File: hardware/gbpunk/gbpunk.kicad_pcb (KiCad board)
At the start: 2 copper layers, 57.5 x 82 mm, 61 parts, among them J1 CART, J2 SWD_CONNECTOR, J4 SWD_CONNECTOR, P1 USB_C_CONNECTOR, SW7 RESET, SW9 USB_BOOT, U1 RP2040, U2 SN74LVC4245A, U3 W25Q128JVS, U4 NCP1117-3.3_SOT223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

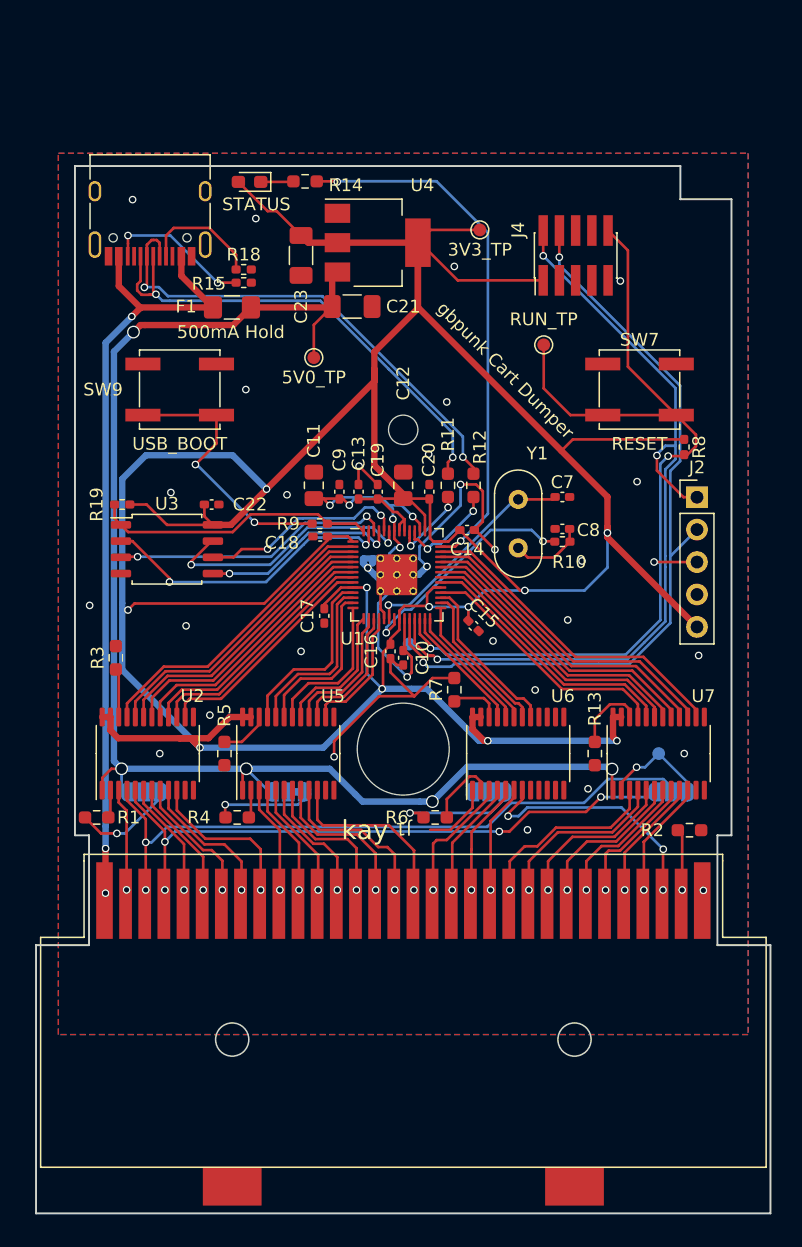
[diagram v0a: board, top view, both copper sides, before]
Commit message: big PCB reroute so the connector is not upside down
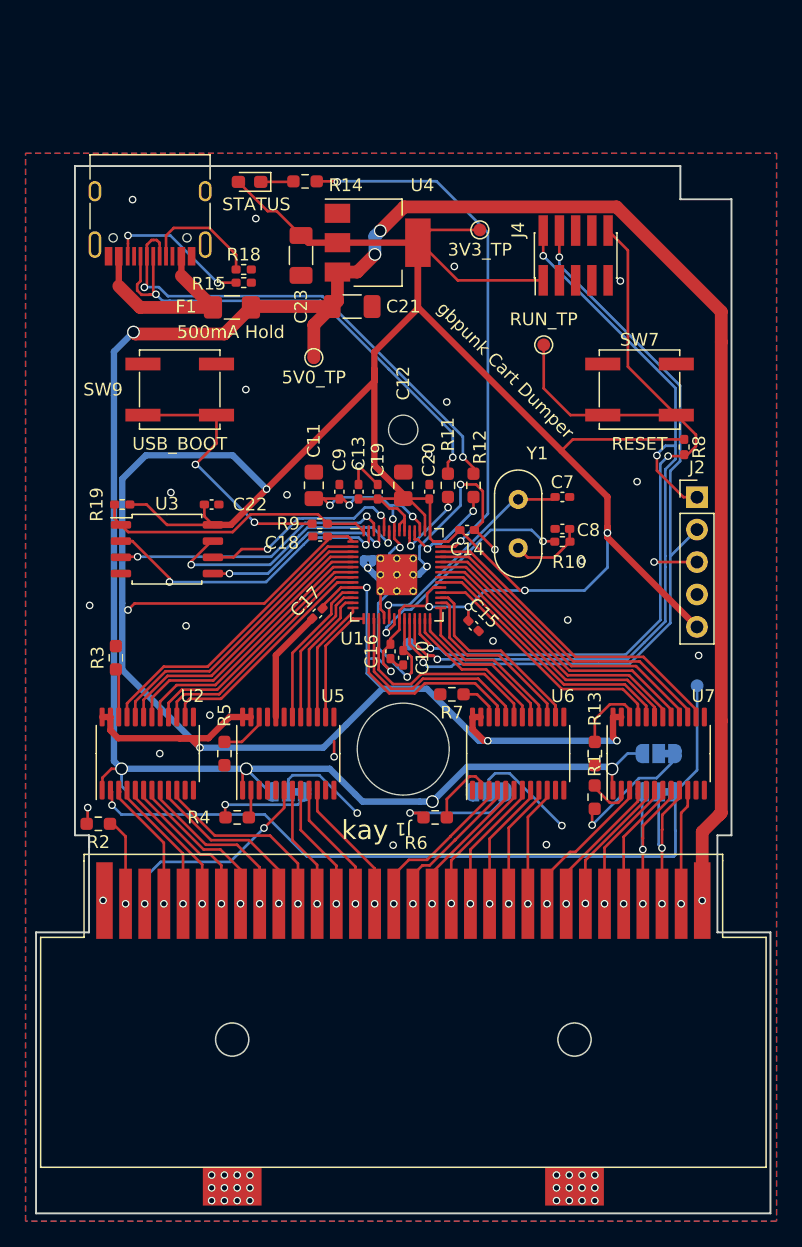
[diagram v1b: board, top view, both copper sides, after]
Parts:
- moved R2 46.3 mm to (76.1, 90.5)
- moved JP2 40.4 mm to (120.0, 85.0)
- moved R1 39.0 mm to (115.0, 88.4), turned to -90 degrees
- moved TP4 6.10 mm to (123.0, 79.7)
- moved JP1 1.00 mm to (120.0, 88.0)
- moved C17 0.57 mm to (93.3, 74.0), turned to -135 degrees
- moved R7 0.41 mm to (103.8, 80.4), turned to 180 degrees
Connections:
- J1 pad 1: VBUS -> +5V
- R2 pad 1: GND -> Net-(J1-Pad31)
- R2 pad 2: Net-(J1-Pad31) -> GND
- U1 pad 11: /A4_L -> /RST_L
- U1 pad 12: /A5_L -> /A15_L
- U1 pad 13: /A6_L -> /A14_L
- U1 pad 14: /A7_L -> /A13_L
- U1 pad 15: /A8_L -> /A12_L
- U1 pad 16: /A9_L -> /A11_L
- U1 pad 18: /A11_L -> /A9_L
- U1 pad 2: /CLK_L -> /D7_L
- U1 pad 27: /A12_L -> /A8_L
- U1 pad 28: /A13_L -> /A7_L
- U1 pad 29: /A14_L -> /A6_L
- U1 pad 3: /~{WR_L} -> /D6_L
- U1 pad 30: /A15_L -> /A5_L
- U1 pad 31: /RST_L -> /A4_L
- U1 pad 32: /D0_L -> /A3_L
- U1 pad 34: /D1_L -> /A2_L
- U1 pad 35: /D2_L -> /A1_L
- U1 pad 36: /D3_L -> /A0_L
- U1 pad 37: /D4_L -> /~{CS_L}
- U1 pad 38: /D5_L -> /~{RD_L}
- U1 pad 39: /D6_L -> /~{WR_L}
- U1 pad 4: /~{RD_L} -> /D5_L
- U1 pad 40: /D7_L -> /CLK_L
- U1 pad 5: /~{CS_L} -> /D4_L
- U1 pad 6: /A0_L -> /D3_L
- U1 pad 7: /A1_L -> /D2_L
- U1 pad 8: /A2_L -> /D1_L
- U1 pad 9: /A3_L -> /D0_L
- U2 pad 10: /A3 -> /D0
- U2 pad 14: /A3_L -> /D0_L
- U2 pad 15: /A2_L -> /D1_L
- U2 pad 16: /A1_L -> /D2_L
- U2 pad 17: /A0_L -> /D3_L
- U2 pad 18: /~{CS_L} -> /D4_L
- U2 pad 19: /~{RD_L} -> /D5_L
- U2 pad 2: Net-(R1-Pad1) -> Net-(JP1-Pad1)
- U2 pad 20: /~{WR_L} -> /D6_L
- U2 pad 21: /CLK_L -> /D7_L
- U2 pad 3: /CLK -> /D7
- U2 pad 4: /~{WR} -> /D6
- U2 pad 5: /~{RD} -> /D5
- U2 pad 6: /~{CS} -> /D4
- U2 pad 7: /A0 -> /D3
- U2 pad 8: /A1 -> /D2
- U2 pad 9: /A2 -> /D1
- U5 pad 10: /A11 -> /A12
- U5 pad 14: /A11_L -> /A12_L
- U5 pad 15: /A10_L -> /A13_L
- U5 pad 16: /A9_L -> /A14_L
- U5 pad 17: /A8_L -> /A15_L
- U5 pad 18: /A7_L -> /RST_L
- U5 pad 19: /A6_L -> GND
- U5 pad 20: /A5_L -> GND
- U5 pad 21: /A4_L -> GND
- U5 pad 3: /A4 -> GND
- U5 pad 4: /A5 -> GND
- U5 pad 5: /A6 -> GND
- U5 pad 6: /A7 -> /RST
- U5 pad 7: /A8 -> /A15
- U5 pad 8: /A9 -> /A14
- U5 pad 9: /A10 -> /A13
- U6 pad 10: GND -> /A4
- U6 pad 14: GND -> /A4_L
- U6 pad 15: GND -> /A5_L
- U6 pad 16: GND -> /A6_L
- U6 pad 17: /RST_L -> /A7_L
- U6 pad 18: /A15_L -> /A8_L
- U6 pad 19: /A14_L -> /A9_L
- U6 pad 20: /A13_L -> /A10_L
- U6 pad 21: /A12_L -> /A11_L
- U6 pad 3: /A12 -> /A11
- U6 pad 4: /A13 -> /A10
- U6 pad 5: /A14 -> /A9
- U6 pad 6: /A15 -> /A8
- U6 pad 7: /RST -> /A7
- U6 pad 8: GND -> /A6
- U6 pad 9: GND -> /A5
- U7 pad 10: /D7 -> /CLK
- U7 pad 14: /D7_L -> /CLK_L
- U7 pad 15: /D6_L -> /~{WR_L}
- U7 pad 16: /D5_L -> /~{RD_L}
- U7 pad 17: /D4_L -> /~{CS_L}
- U7 pad 18: /D3_L -> /A0_L
- U7 pad 19: /D2_L -> /A1_L
- U7 pad 2: Net-(JP1-Pad1) -> Net-(R1-Pad1)
- U7 pad 20: /D1_L -> /A2_L
- U7 pad 21: /D0_L -> /A3_L
- U7 pad 3: /D0 -> /A3
- U7 pad 4: /D1 -> /A2
- U7 pad 5: /D2 -> /A1
- U7 pad 6: /D3 -> /A0
- U7 pad 7: /D4 -> /~{CS}
- U7 pad 8: /D5 -> /~{RD}
- U7 pad 9: /D6 -> /~{WR}
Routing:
- net +5V: track 118.1 -> 198.8 mm, vias 5 -> 8
- net Net-(JP1-Pad1): track 8.41 -> 61.4 mm
- net VBUS: track 62.4 -> 15.4 mm, vias 4 -> 0
- net /~{WR}: track 52.3 -> 14.6 mm
- net /~{RD}: track 48.8 -> 14.3 mm, vias 4 -> 2
- net GND: track 64.3 -> 75.5 mm, vias 29 -> 54
- net /A11_L: track 10.2 -> 16.9 mm
- net /A9_L: track 10.7 -> 17.4 mm
- net /A10_L: track 10.5 -> 17.1 mm
- net /RST: track 19.5 -> 16.6 mm, vias 3 -> 2
- net Net-(JP2-Pad1): track 8.05 -> 10.5 mm
- net Net-(J1-Pad31): track 4.82 -> 6.89 mm
- net /D1_L: track 21.0 -> 19.0 mm
- net /A2_L: track 19.0 -> 21.0 mm
- net /D2_L: track 21.7 -> 19.8 mm
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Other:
- outline, holes or cut-outs redrawn

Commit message: updated the board
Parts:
- added G***: LOGO, gbpunk:sussy, F.Cu at (85.8, 74.7)
- added G***: LOGO, gbpunk:cart, B.Cu at (86.0, 66.3)
- added G***: LOGO, gbpunk:logo, B.Cu at (99.8, 109.6)
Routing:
- net GND: track 75.5 -> 82.2 mm, vias 54 -> 57
- net +1V1: track 34.8 -> 32.6 mm
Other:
- board text added: "3V3"
- board text added: "A message to all aspiring engineers: Don't worry. I don't know what I'm doing either"
- board text added: "DO CRIMES"
- board text added: "GND"
- board text added: "HACK THE PLANET"
- board text added: "I don't wanna go to work I just wanna learn about esoteric gameboy mappers"
- board text added: "MORE NONSENSE HERE KIDOUTAI.COM"
- board text added: "RST"
- board text added: "SWCLK"
- board text added: "SWDIO"
- board text added: "V2.0"
- board text added: "Works Cited: github.com/Gekkio mgba-emu.github.io/gbdoc/ gbdev.gg8.se"
- board text added: "You wage wars, murder, cheat, lie to us and try to make us believe it's for our own good, yet we're the criminals. Yes, I am a criminal. My crime is that of curiosity."
- board text removed: "thank you gekkio! Works Cited: https://github.com/Gekkio"

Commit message: orderd boards for V2
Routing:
- net GND: track 82.2 -> 92.8 mm, vias 57 -> 64
- net /D7_L: track 23.8 -> 30.3 mm
- net (no net): track 3.83 -> 0.00 mm
- net /USB_DP: track 34.1 -> 37.6 mm
- net +5V: track 198.8 -> 199.4 mm, vias 8 -> 7
- net /USB_DM: track 37.8 -> 38.0 mm, vias 2 -> 3
- net /D7: track 10.5 -> 10.4 mm, vias 1 -> 0
- net /A10: track 12.1 -> 12.0 mm, vias 1 -> 0
- net Net-(J1-Pad31): vias 1 -> 0
- net /~{WR}: vias 2 -> 1
- net /~{RD}: vias 2 -> 1
- net /~{CS}: vias 1 -> 0
- net /D6: vias 1 -> 0
- net /D5: vias 1 -> 0
- net /D4: vias 1 -> 0
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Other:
- board text added: "Works Cited: github.com/Gekkio mgba-emu.github.io/gbdoc gbdev.gg8.se"
- board text removed: "Works Cited: github.com/Gekkio mgba-emu.github.io/gbdoc/ gbdev.gg8.se"

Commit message: stuff
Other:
- board text added: "1V1"
- board text added: "5V"
- board text added: "RESET"
- board text added: "RUN"
- board text added: "USB BOOT"

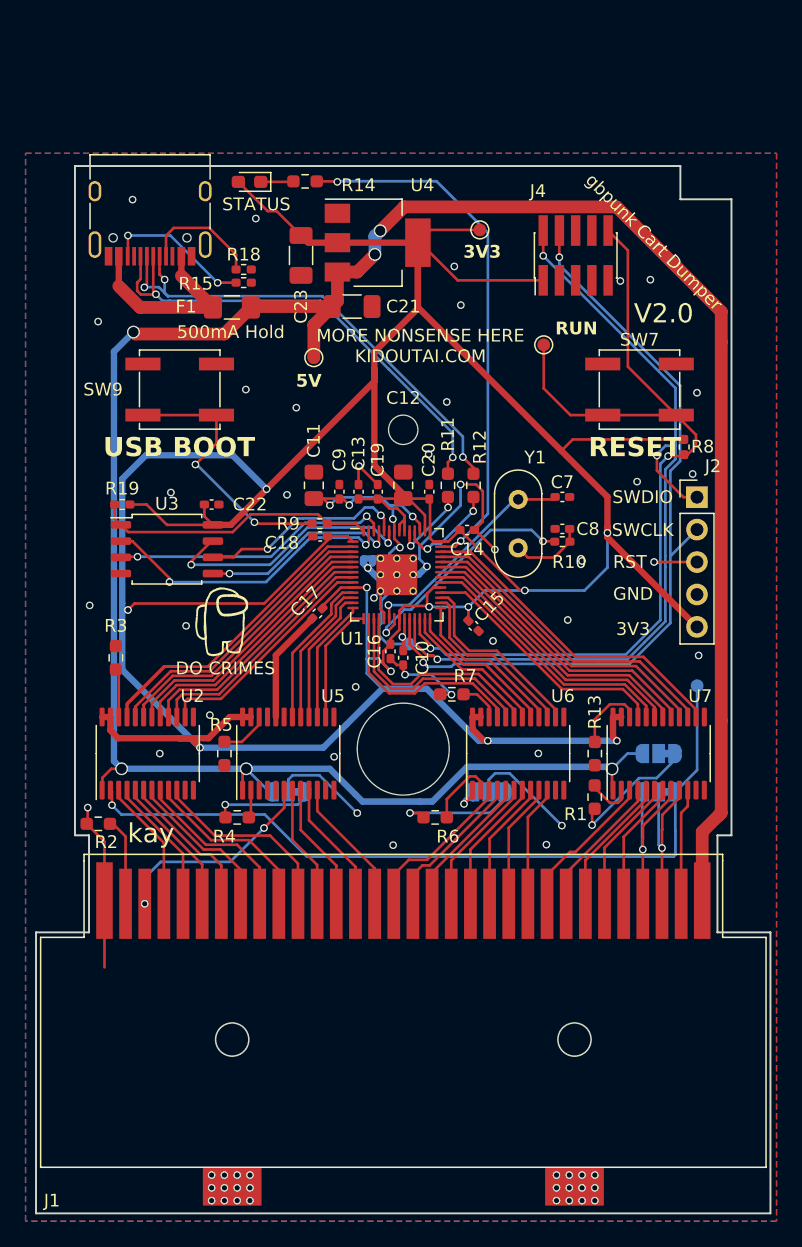
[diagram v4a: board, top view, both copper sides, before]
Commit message: added detection circuit and voltage switching for GBA/GB
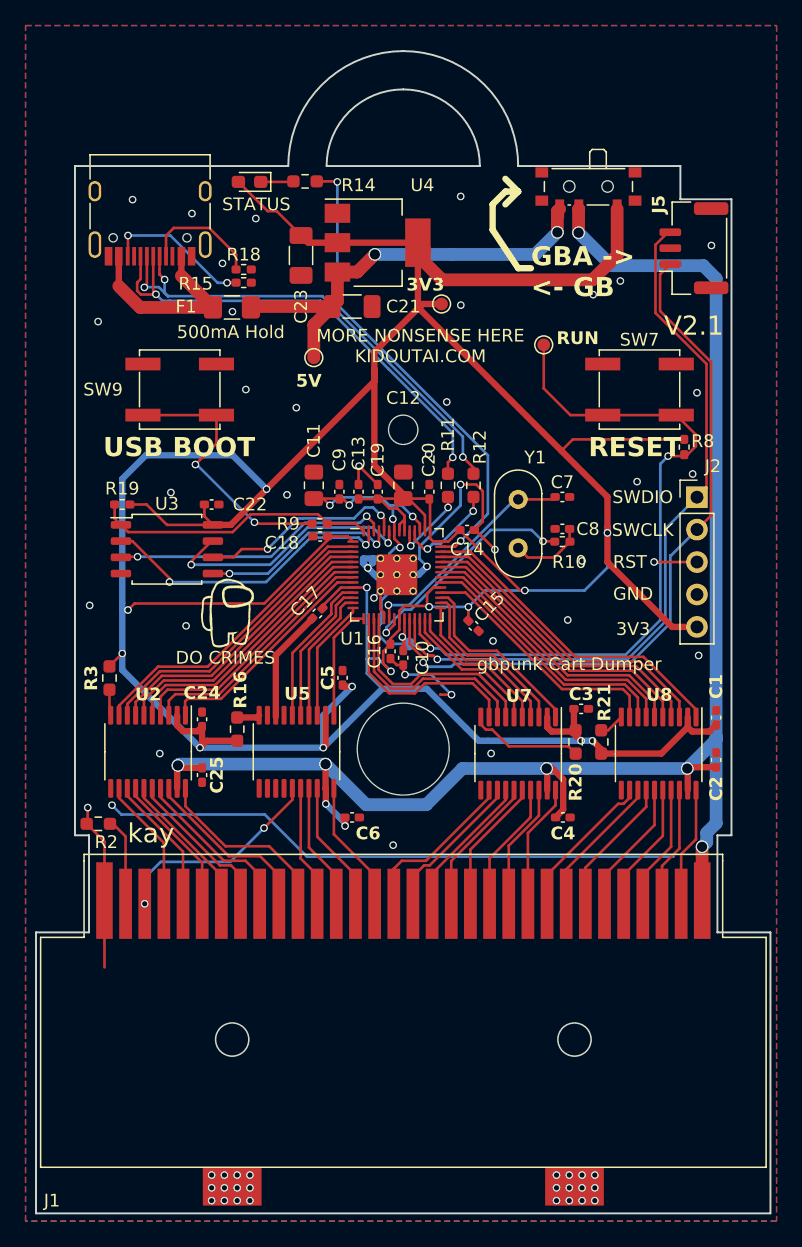
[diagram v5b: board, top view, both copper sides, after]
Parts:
- removed J4: SWD_CONNECTOR, Connector_PinHeader_1.27mm:PinHeader_2x05_P1.27mm_Vertical_SMD
- removed JP1, JP3, JP4: SWDIR_1, Jumper:SolderJumper-3_P1.3mm_Bridged12_RoundedPad1.0x1.5mm
- removed JP2: SWDIR_0, Jumper:SolderJumper-3_P1.3mm_Bridged12_RoundedPad1.0x1.5mm
- removed R1, R13, R4, R5, R6, R7: 1k, Resistor_SMD:R_0603_1608Metric_Pad0.98x0.95mm_HandSolder
- removed TP4: DBUS_DIR_TP, TestPoint:TestPoint_Pad_D1.0mm
- removed U6: SN74LVC4245A, Package_SO:TSSOP-24_4.4x7.8mm_P0.65mm
- added C1: 100nF, Capacitor_SMD:C_0402_1005Metric_Pad0.74x0.62mm_HandSolder, F.Cu at (124.5, 82.2)
- added C2: 100nF, Capacitor_SMD:C_0402_1005Metric_Pad0.74x0.62mm_HandSolder, F.Cu at (124.5, 85.5)
- added C24: 100nF, Capacitor_SMD:C_0402_1005Metric_Pad0.74x0.62mm_HandSolder, F.Cu at (84.2, 82.3)
- added C25: 100nF, Capacitor_SMD:C_0402_1005Metric_Pad0.74x0.62mm_HandSolder, F.Cu at (84.2, 86.7)
- added C3: 100nF, Capacitor_SMD:C_0402_1005Metric_Pad0.74x0.62mm_HandSolder, F.Cu at (113.9, 81.5)
- added C4: 100nF, Capacitor_SMD:C_0402_1005Metric_Pad0.74x0.62mm_HandSolder, F.Cu at (112.5, 90.0)
- added C5: 100nF, Capacitor_SMD:C_0402_1005Metric_Pad0.74x0.62mm_HandSolder, F.Cu at (95.2, 79.1)
- added C6: 100nF, Capacitor_SMD:C_0402_1005Metric_Pad0.74x0.62mm_HandSolder, F.Cu at (96.0, 90.0)
- added J5: DEBUG_CONNECTOR, Connector_JST:JST_GH_SM03B-GHS-TB_1x03-1MP_P1.25mm_Horizontal, F.Cu at (122.8, 45.4)
- added R16: 1k, Resistor_SMD:R_0603_1608Metric_Pad0.98x0.95mm_HandSolder, F.Cu at (87.0, 83.1)
- added R20: 1k, Resistor_SMD:R_0603_1608Metric_Pad0.98x0.95mm_HandSolder, F.Cu at (113.5, 84.1)
- added R21: 1k, Resistor_SMD:R_0603_1608Metric_Pad0.98x0.95mm_HandSolder, F.Cu at (115.5, 84.1)
- added SW1: CART_SELECT, Button_Switch_SMD:SW_SPDT_PCM12, F.Cu at (114.5, 40.9)
- added U8: TXS0108EPW, Package_SO:TSSOP-20_4.4x6.5mm_P0.65mm, F.Cu at (120.0, 85.0)
- U2, U5, U7: value SN74LVC4245A -> TXS0108EPW; footprint Package_SO:TSSOP-24_4.4x7.8mm_P0.65mm -> Package_SO:TSSOP-20_4.4x6.5mm_P0.65mm
- moved U7 11.0 mm to (109.0, 85.0), turned to -90 degrees
- moved TP3 6.53 mm to (103.0, 49.8)
- moved R3 1.66 mm to (77.0, 79.1)
- moved G*** 0.82 mm to (86.2, 74.0)
- moved U5 0.66 mm to (91.6, 84.9), turned to -90 degrees
- moved U2 0.14 mm to (80.0, 84.9), turned to -90 degrees
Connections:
- J1 pad 1: +5V -> /CART_VCC
- R3 pad 1: Net-(R3-Pad1) -> Net-(U2-OE)
- R3 pad 2: GND -> +3.3V
- U2 pad 1: +5V -> /D0_L
- U2 pad 10: /D0 -> Net-(U2-OE)
- U2 pad 12: GND -> /D7
- U2 pad 13: GND -> /D6
- U2 pad 14: /D0_L -> /D5
- U2 pad 15: /D1_L -> /D4
- U2 pad 16: /D2_L -> /D3
- U2 pad 17: /D3_L -> /D2
- U2 pad 18: /D4_L -> /D1
- U2 pad 19: /D5_L -> /CART_VCC
- U2 pad 2: Net-(JP1-Pad1) -> +3.3V
- U2 pad 20: /D6_L -> /D0
- U2 pad 3: /D7 -> /D1_L
- U2 pad 4: /D6 -> /D2_L
- U2 pad 5: /D5 -> /D3_L
- U2 pad 6: /D4 -> /D4_L
- U2 pad 7: /D3 -> /D5_L
- U2 pad 8: /D2 -> /D6_L
- U2 pad 9: /D1 -> /D7_L
- U5 pad 1: +5V -> /A12_L
- U5 pad 10: /A12 -> Net-(U5-OE)
- U5 pad 14: /A12_L -> GND
- U5 pad 15: /A13_L -> /RST
- U5 pad 16: /A14_L -> /A15
- U5 pad 17: /A15_L -> /A14
- U5 pad 18: /RST_L -> /A13
- U5 pad 19: GND -> /CART_VCC
- U5 pad 2: Net-(R4-Pad1) -> +3.3V
- U5 pad 20: GND -> /A12
- U5 pad 3: GND -> /A13_L
- U5 pad 4: GND -> /A14_L
- U5 pad 5: GND -> /A15_L
- U5 pad 6: /RST -> /RST_L
- U5 pad 7: /A15 -> GND
- U5 pad 8: /A14 -> GND
- U5 pad 9: /A13 -> GND
- U7 pad 1: +5V -> /A4_L
- U7 pad 10: /CLK -> Net-(U7-OE)
- U7 pad 12: GND -> /A11
- U7 pad 13: GND -> /A10
- U7 pad 14: /CLK_L -> /A9
- U7 pad 15: /~{WR_L} -> /A8
- U7 pad 16: /~{RD_L} -> /A7
- U7 pad 17: /~{CS_L} -> /A6
- U7 pad 18: /A0_L -> /A5
- U7 pad 19: /A1_L -> /CART_VCC
- U7 pad 2: Net-(R1-Pad1) -> +3.3V
- U7 pad 20: /A2_L -> /A4
- U7 pad 3: /A3 -> /A5_L
- U7 pad 4: /A2 -> /A6_L
- U7 pad 5: /A1 -> /A7_L
- U7 pad 6: /A0 -> /A8_L
- U7 pad 7: /~{CS} -> /A9_L
- U7 pad 8: /~{RD} -> /A10_L
- U7 pad 9: /~{WR} -> /A11_L
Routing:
- net +5V: track 199.4 -> 34.3 mm, vias 7 -> 2
- net /CART_VCC: track 0.00 -> 129.6 mm, vias 0 -> 8
- net Net-(JP1-Pad1): track 61.0 -> 0.00 mm, vias 1 -> 0
- net GND: track 92.8 -> 122.3 mm, vias 64 -> 63
- net +3.3V: track 318.4 -> 336.0 mm, vias 11 -> 14
- net /RUN: track 75.7 -> 59.0 mm
- net Net-(JP2-Pad1): track 10.5 -> 0.00 mm, vias 1 -> 0
- net Net-(JP4-Pad1): track 9.63 -> 0.00 mm, vias 1 -> 0
- net Net-(U7-OE): track 0.00 -> 8.96 mm
- net /SWDIO: track 65.7 -> 57.3 mm, vias 3 -> 1
- net Net-(JP3-Pad1): track 7.94 -> 0.00 mm, vias 1 -> 0
- net /SWCLK: track 62.7 -> 56.2 mm, vias 2 -> 1
- net /D7_L: track 30.3 -> 24.2 mm
- net Net-(R13-Pad1): track 5.73 -> 0.00 mm
- net Net-(R6-Pad1): track 5.66 -> 0.00 mm
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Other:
- board size 57.5 x 82 mm -> 57.5 x 91 mm
- board text added: "GBA -> <- GB"
- board text added: "V2.1"
- board text removed: "V2.0"
